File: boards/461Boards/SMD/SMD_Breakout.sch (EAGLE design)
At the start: 7 parts, among them U1 ATTINY461A-SUATTINY461A-QFN

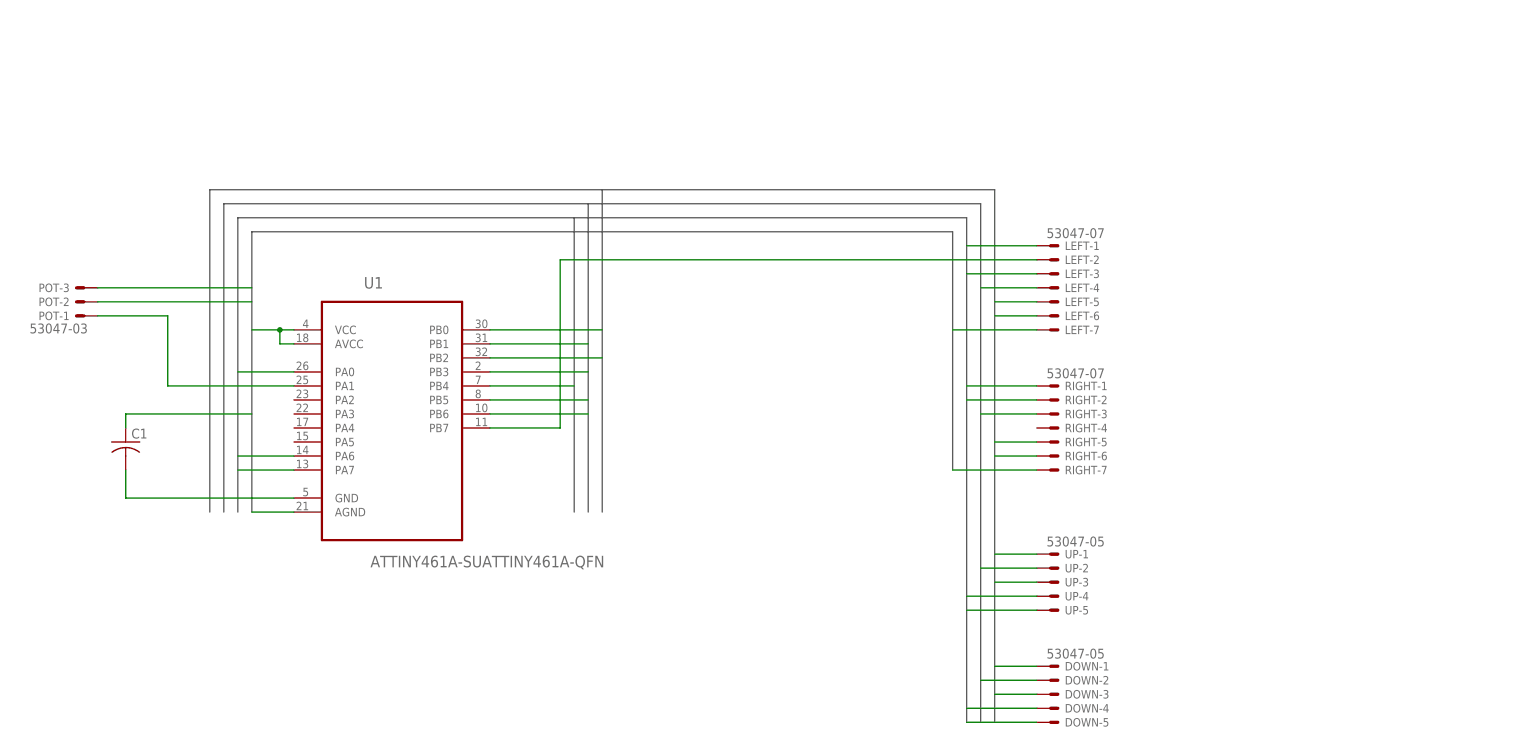
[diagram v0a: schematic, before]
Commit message: SMD Breakout with layout complete ( all pins to the frame board with global reset). Board progress issue updated with pinouts and layout guide for design review.
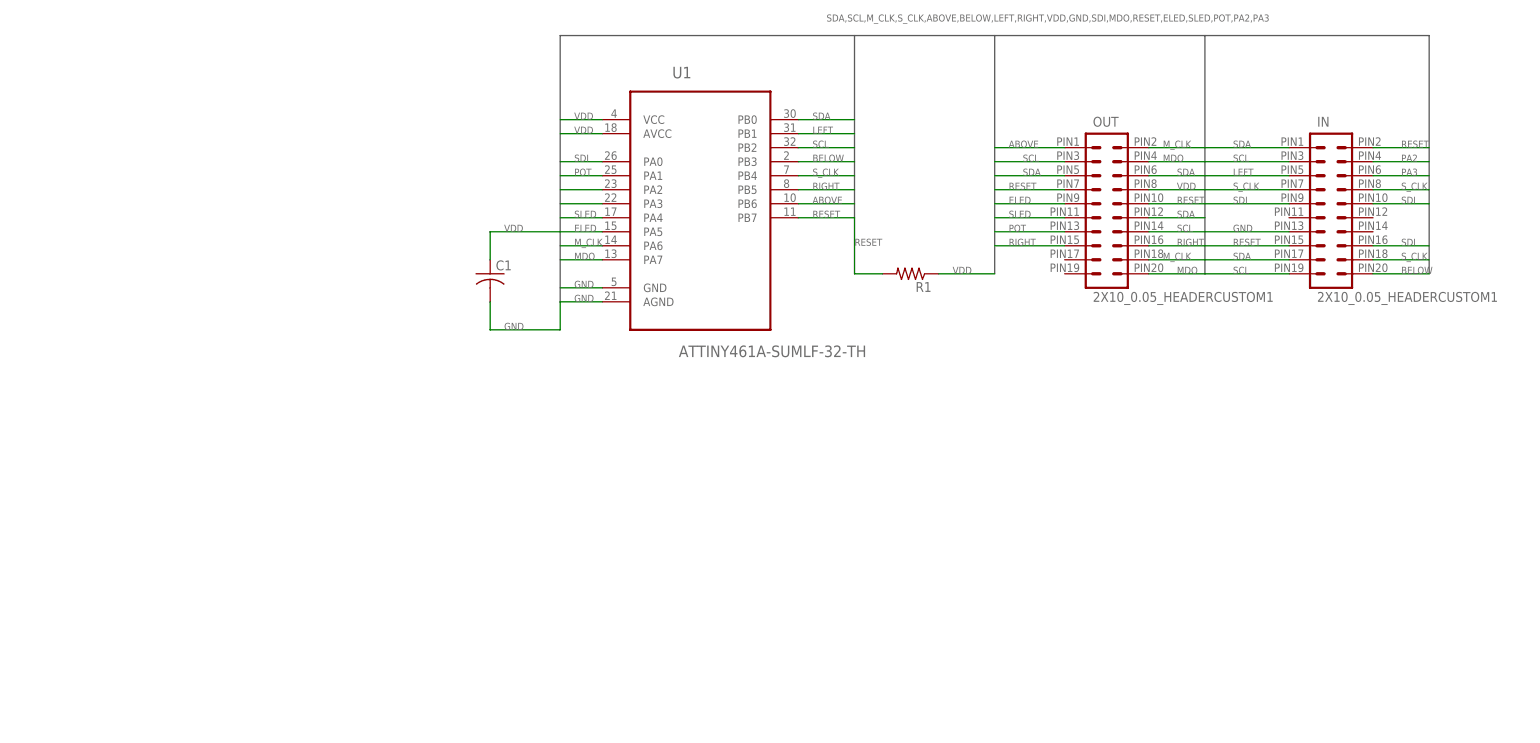
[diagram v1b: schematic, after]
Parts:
- removed DOWN, UP: 53047-05, con-molex:53047-05
- removed LEFT, RIGHT: 53047-07, con-molex:53047-07
- removed POT: 53047-03, con-molex:53047-03
- added IN, OUT: 2X10_0.05_HEADERCUSTOM1, Custom:2X10_0.05_HEADERCUSTOM1
- added R1: (no value), rcl:R-US_R0603
- U1: value ATTINY461A-SUATTINY461A-QFN -> ATTINY461A-SUMLF-32-TH; device Atmel_By_element14_Batch_1-00:ATTINY461A-SUATTINY461A-QFN -> Atmel_By_element14_Batch_1-00:ATTINY461A-SUMLF-32-TH
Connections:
- removed net CLK_IN: DOWN-4.S, LEFT-3.S, U1.PB4
- removed net CLK_OUT: RIGHT-2.S, U1.PA6, UP-4.S
- removed net DOWN: DOWN-2.S, U1.PB3
- removed net N$1: LEFT-2.S, U1.PB7
- removed net N$2: POT-1.S, U1.PA1
- removed net UP: U1.PB6, UP-2.S
- new net ABOVE: OUT.1, U1.PB6
- new net BELOW: IN.20, U1.PB3
- new net ELED: OUT.9, U1.PA5
- new net M_CLK: OUT.18, OUT.2, U1.PA6
- new net PA2: IN.4, U1.PA2
- new net PA3: IN.6, U1.PA3
- new net POT: OUT.13, U1.PA1
- new net RESET: IN.15, IN.2, OUT.10, OUT.7, R1.2, U1.PB7
- new net SLED: OUT.11, U1.PA4
- new net S_CLK: IN.18, IN.7, IN.8, U1.PB4
- net GND: now also IN.13; no longer POT-2.S, RIGHT-7.S
- net LEFT: now also IN.5; no longer LEFT-4.S
- net MDO: now also OUT.20, OUT.4; no longer RIGHT-1.S, UP-5.S
- net RIGHT: now also OUT.15, OUT.16; no longer RIGHT-3.S
- net SCL: now also IN.19, IN.3, OUT.14, OUT.3; no longer DOWN-3.S, LEFT-6.S, RIGHT-6.S, UP-3.S
- net SDA: now also IN.1, IN.17, OUT.12, OUT.5, OUT.6; no longer DOWN-1.S, LEFT-5.S, RIGHT-5.S, UP-1.S
- net SDI: now also IN.10, IN.16, IN.9; no longer DOWN-5.S, LEFT-1.S
- net VDD: now also OUT.8, R1.1; no longer LEFT-7.S, POT-3.S
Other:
- moved on the sheet: C1, U1
